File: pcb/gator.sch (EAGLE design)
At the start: 117 parts, among them J2 POWER_JACKPTH, X1 USB-A-S, Y1 12MHz

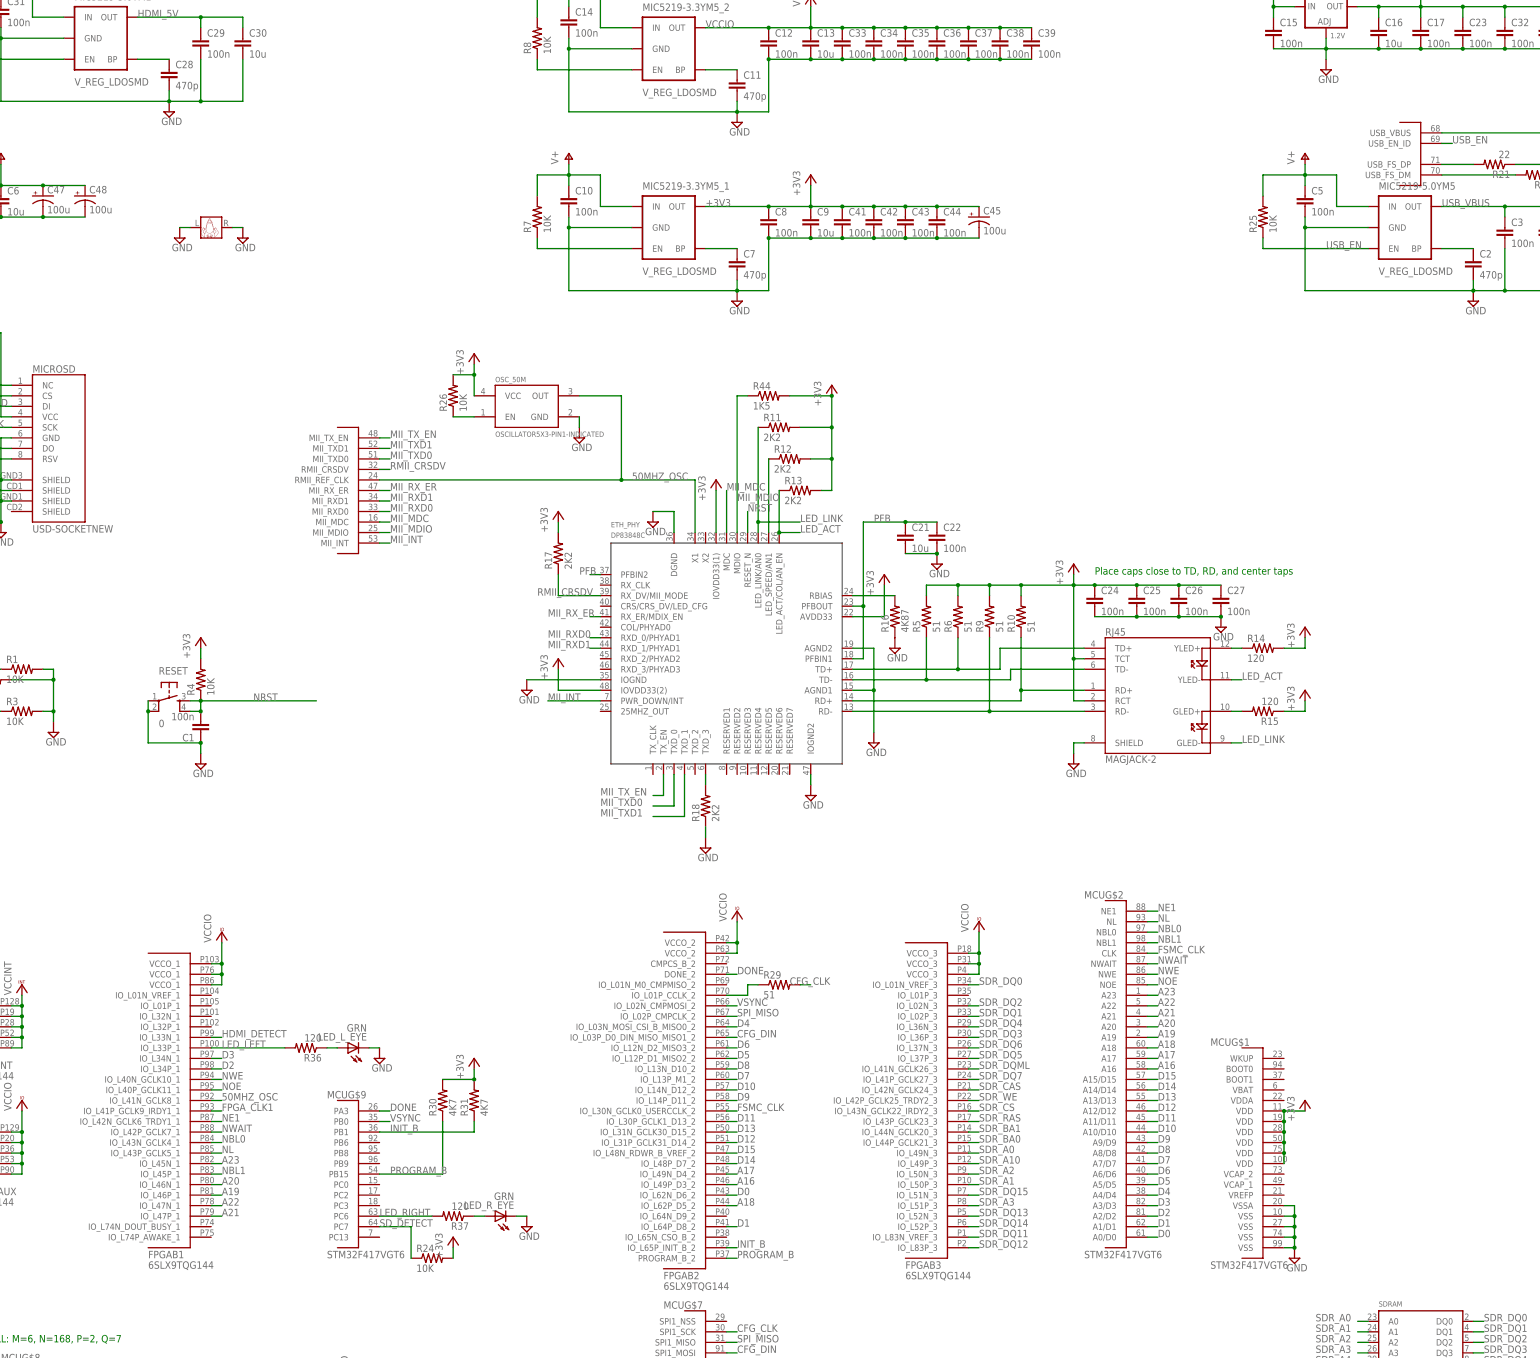
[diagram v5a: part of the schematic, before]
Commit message: Added Digikey parts for everything except resistors and capacitors
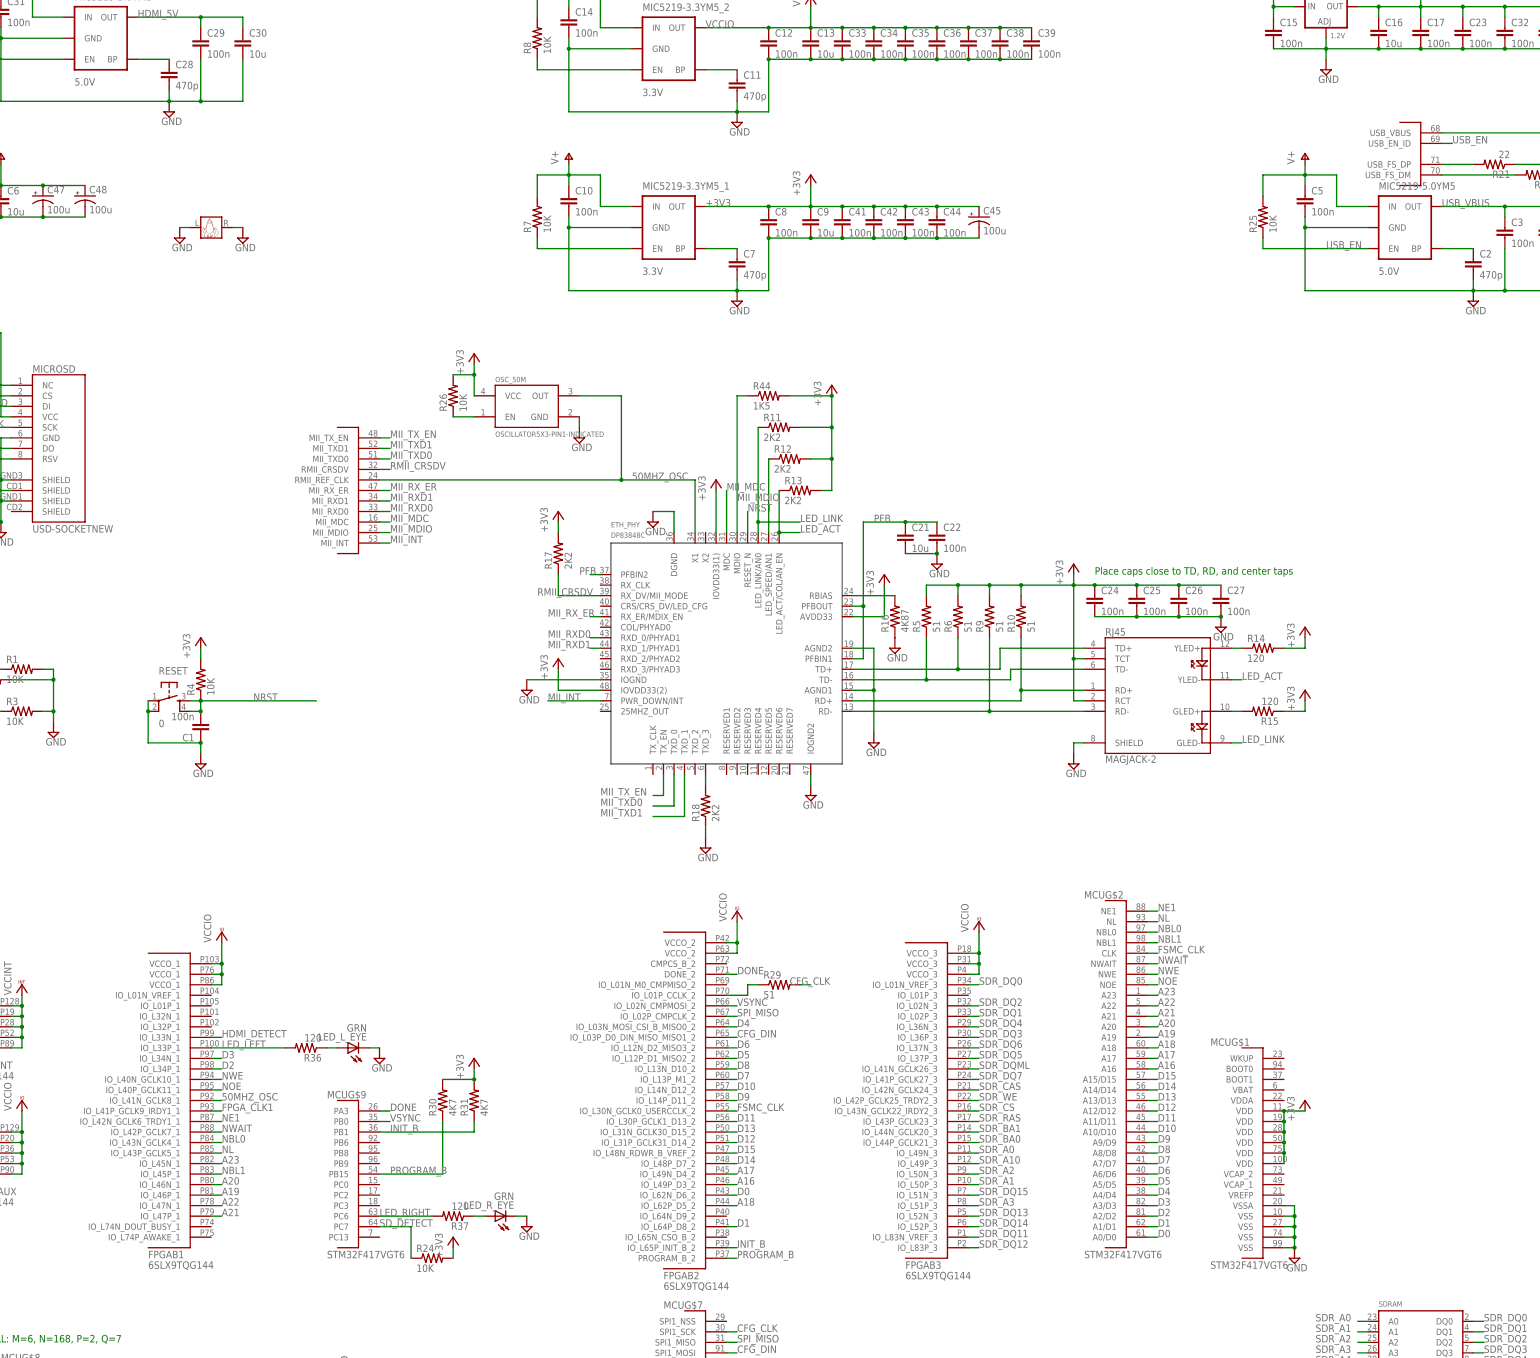
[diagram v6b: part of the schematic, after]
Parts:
- D1: DIGIKEY# (none) -> 497-6588-1-ND; MANF (none) -> STMicroelectronics; MANF# (none) -> STPS5L40RL
- ETH_PHY: DIGIKEY# (none) -> DP83848CVVX/NOPBCT-ND; MANF (none) -> Texas Instruments; MANF# (none) -> DP83848CVVX/NOPB; MOUSER# (none) -> 926-DP83848CVVX/NOPB
- FPGA: DIGIKEY# (none) -> 122-1745-ND; MANF (none) -> Xilinx Inc; MANF# (none) -> XC6SLX9-2TQG144C
- FPGA_JTAG: DIGIKEY# (none) -> AE10561-ND; MANF (none) -> Assmann WSW Components; MANF# (none) -> AWHW2-14G-0202-T-R
- J2: DIGIKEY# (none) -> CP-002A-ND; MANF (none) -> CUI Inc; MANF# (none) -> PJ-002A
- JTAG: DIGIKEY# (none) -> S9172-ND; MANF (none) -> Sullins Connector Solutions; MANF# (none) -> SBH11-PBPC-D10-ST-BK
- LED_L_EYE, LED_R_EYE: DIGIKEY# (none) -> 160-1659-ND; MANF (none) -> Lite-On Inc; MANF# (none) -> LTL1CHKGKNN
- MCU: DIGIKEY# (none) -> 497-11900-ND; MANF (none) -> STMicroelectronics; MANF# (none) -> STM32F417VGT6
- MIC5219-3.3YM5_1, MIC5219-3.3YM5_2: value V_REG_LDOSMD -> 3.3V; DIGIKEY# (none) -> 576-1281-1-ND; MANF (none) -> Micrel Inc; MANF# (none) -> MIC5219-3.3YM5 TR
- MIC5219-5.0YM1, MIC5219-5.0YM5: value V_REG_LDOSMD -> 5.0V; DIGIKEY# (none) -> 576-2770-1-ND; MANF (none) -> Micrel Inc; MANF# (none) -> MIC5219-5.0YM5 TR
- MICROSD: DIGIKEY# (none) -> 101-00660-68-6-1-ND; MANF (none) -> Amphenol Commercial Products; MANF# (none) -> 101-00660-68-6
- NCP565ST12T3G: DIGIKEY# (none) -> NCP565ST12T3GOSCT-ND; MANF (none) -> ON Semiconductor; MANF# (none) -> NCP565ST12T3G
- OSC_50M: DIGIKEY# (none) -> CTX1011CT-ND; MANF (none) -> CTS-Frequency Controls; MANF# (none) -> 636L3C050M00000
- R27, R28: DIGIKEY# (none) -> YC164J-51CT-ND; MANF (none) -> Yageo; MANF# (none) -> YC164-JR-0751RL
- RJ45: DIGIKEY# (none) -> 380-1103-ND; MANF (none) -> Stewart Connector; MANF# (none) -> SI-50170-F
- SDRAM: DIGIKEY# (none) -> 557-1223-1-ND; MANF (none) -> Micron Technology Inc; MANF# (none) -> MT48LC16M16A2P-6A:D TR; MOUSER# (none) -> 913-AS4C16M16S-6TAN
- U$2: DIGIKEY# (none) -> WM19084CT-ND; MANF (none) -> Molex Inc; MANF# (none) -> 5002541927
- U$3: DIGIKEY# (none) -> 568-4770-1-ND; MANF (none) -> NXP Semiconductors; MANF# (none) -> PCA9527DP,118
- U$4: DIGIKEY# (none) -> T1065-P5P-ND; MANF (none) -> CUI Inc; MANF# (none) -> ETSA060200UDC-P5P-SZ
- X1: DIGIKEY# (none) -> 1175-1016-ND; MANF (none) -> CNC Tech; MANF# (none) -> 1002-002-01100
- Y1: DIGIKEY# (none) -> CTX904-ND; MANF (none) -> CTS-Frequency Controls; MANF# (none) -> ATS120B

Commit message: Finished adding DigiKey part numbers to schematic
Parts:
- C1, C10, C12, C14, C15, C17, C22, C23, C24, C25, C26, C27, C29, C3, C31, C32, C33, C34, C35, C36, C37, C38, C39, C40, C41, C42, C43, C44, C49, C5, C8: DIGIKEY# (none) -> 445-1316-1-ND; MANF (none) -> TDK Corporation; MANF# (none) -> C1608X7R1E104K080AA
- C11, C2, C28, C7: DIGIKEY# (none) -> 445-1289-1-ND; MANF (none) -> TDK Corporation; MANF# (none) -> C1608C0G1H471J080AA
- C13, C16, C20, C21, C30, C4, C6, C9: DIGIKEY# (none) -> 445-6853-1-ND; MANF (none) -> TDK Corporation; MANF# (none) -> C1608X5R1A106M080AC
- C18, C19: DIGIKEY# (none) -> 490-1410-1-ND; MANF (none) -> Murata Electronics North America; MANF# (none) -> GRM1885C1H200JA01D
- C45, C46, C47, C48: DIGIKEY# (none) -> 1189-1247-ND; MANF (none) -> Rubycon; MANF# (none) -> 25ZLJ150M6.3X11
- J2: DIGIKEY# CP-002A-ND -> CP-002AH-ND; MANF# PJ-002A -> PJ-002AH
- R1, R2, R23, R24, R25, R26, R3, R34, R35, R4, R7, R8: DIGIKEY# (none) -> RMCF0603JT10K0CT-ND; MANF (none) -> Stackpole Electronics Inc; MANF# (none) -> RMCF0603JT10K0
- R10, R29, R5, R6, R9: DIGIKEY# (none) -> RMCF0603JT51R0CT-ND; MANF (none) -> Stackpole Electronics Inc; MANF# (none) -> RMCF0603JT51R0
- R11, R12, R13, R17, R18: DIGIKEY# (none) -> RMCF0603JT2K20CT-ND; MANF (none) -> Stackpole Electronics Inc; MANF# (none) -> RMCF0603JT2K20
- R14, R15, R36, R37: DIGIKEY# (none) -> RMCF0603JT120RCT-ND; MANF (none) -> Stackpole Electronics Inc; MANF# (none) -> RMCF0603JT120R
- R16: DIGIKEY# (none) -> RMCF0603FT4K87CT-ND; MANF (none) -> Stackpole Electronics Inc; MANF# (none) -> RMCF0603FT4K87
- R19, R20, R30, R31: DIGIKEY# (none) -> RMCF0603JT4K70CT-ND; MANF (none) -> Stackpole Electronics Inc; MANF# (none) -> RMCF0603JT4K70
- R21, R22, R32, R33: DIGIKEY# (none) -> RMCF0603JT22R0CT-ND; MANF (none) -> Stackpole Electronics Inc; MANF# (none) -> RMCF0603JT22R0
- R38, R39, R40, R41, R42, R43: DIGIKEY# (none) -> RMCF0603JT47K0CT-ND; MANF (none) -> Stackpole Electronics Inc; MANF# (none) -> RMCF0603JT47K0
- R44: DIGIKEY# (none) -> RMCF0603JT1K50CT-ND; MANF (none) -> Stackpole Electronics Inc; MANF# (none) -> RMCF0603JT1K50
- RESET: DIGIKEY# (none) -> 450-1804-ND; MANF (none) -> TE Connectivity; MANF# (none) -> 1825910-7
